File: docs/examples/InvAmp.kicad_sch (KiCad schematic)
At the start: 5 parts, among them U1 OPAMP

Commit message: ERC-clean KiCad export: project + sym-lib-table, test points on open ports, automatic PWR_FLAGs from geometry nets; ERC (errors+warnings) asserted in tests
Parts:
- added TP1, TP2: TestPoint, symbol Connector:TestPoint
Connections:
- net E0: now also TP1.1
- net W0: now also TP2.1

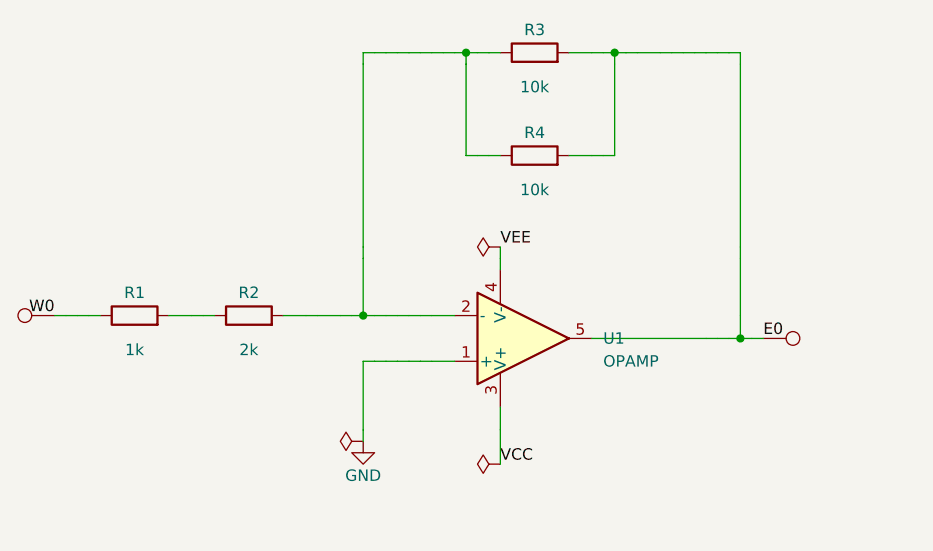
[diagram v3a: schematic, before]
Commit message: Power-net labels drawn as power symbols (registry), axis-flip tie-break (mirror before 180 deg), rotated()/mirrored() API, readable mirror y in JSON; sgen uses <GND> and PS<in> with no explicit orientation
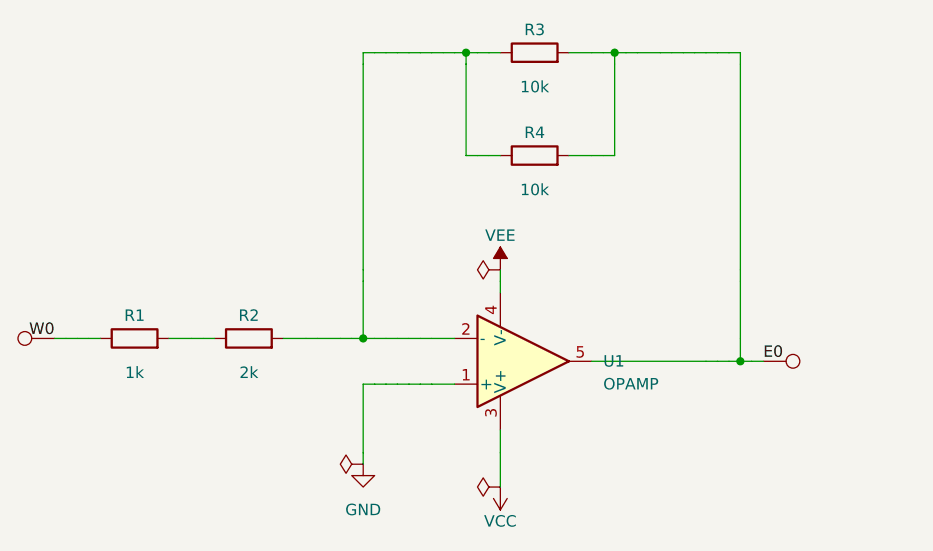
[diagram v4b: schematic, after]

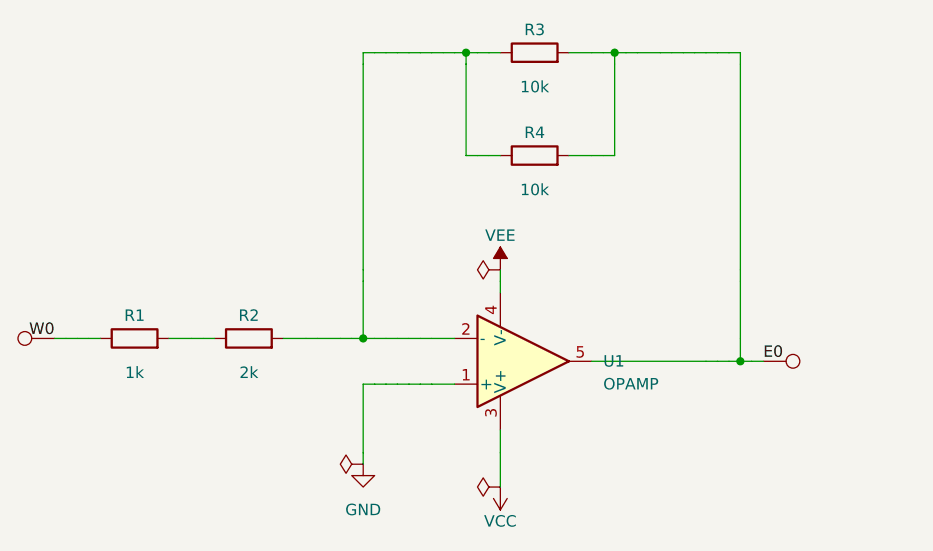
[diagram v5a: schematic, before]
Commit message: Docs: minimal README (abstract, concepts, short syntax, binding, layout, export, skill, examples) + SPEC.md with the full reference; errata: separate arrow examples, >Q2Q2> invalid as duplicate arrow; INV_AMP example uses {in}/{out} and [GND]
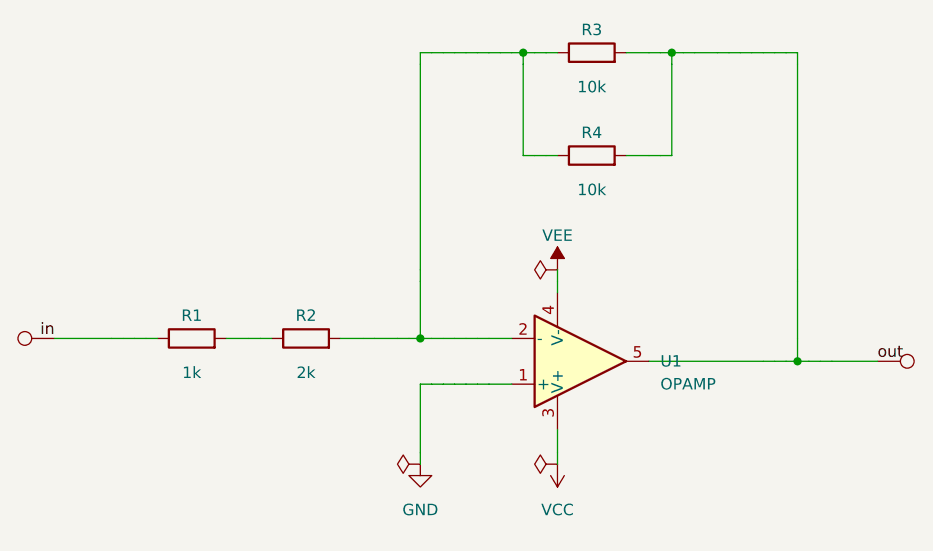
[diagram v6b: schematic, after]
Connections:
- net E0 renamed out
- net W0 renamed in
